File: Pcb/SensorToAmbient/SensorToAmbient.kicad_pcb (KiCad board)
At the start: 2 copper layers, 14 parts, among them J1 Conn_01x04, J2 Conn_01x04, J3 Conn_01x04, J4 Conn_01x06, J5 Conn_01x02, J6 Conn_01x06, J7 Conn_01x04, J8 Conn_01x04, J9 Conn_01x04

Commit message: Making boardedge and spacer holes
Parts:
- added REF**: MountingHole_3mm, Mounting_Holes:MountingHole_3mm, F.Cu at (26.2, 84.6)
- added REF**: MountingHole_3mm, Mounting_Holes:MountingHole_3mm, F.Cu at (67.8, 35.8)
- moved R2 114.0 mm to (42.2, 66.3)
- moved R1 99.0 mm to (42.2, 73.2)
- moved J8 96.8 mm to (61.4, 73.4)
- moved J5 96.3 mm to (45.0, 81.1)
- moved J9 94.7 mm to (61.3, 57.8)
- moved RTC1 92.5 mm to (42.2, 53.1), turned to 90 degrees
- moved J7 90.9 mm to (61.3, 43.6)
- moved 3SB1 77.9 mm to (54.9, 32.4)
- moved J6 74.5 mm to (51.8, 23.3)
- moved DCDC1 73.7 mm to (46.4, 72.3)
- moved J4 67.1 mm to (28.1, 23.3)
- moved J3 63.1 mm to (31.4, 73.5)
- moved J2 55.1 mm to (31.4, 58.3)
- moved J1 53.6 mm to (31.4, 43.2)
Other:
- board outline added: 161.9 x 69.7 mm

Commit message: Complete of footprint layout before first wiring work
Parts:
- removed the J5 at (45.0, 81.1)
- added J7: Conn_01x02, Connectors_JST:JST_XH_S02B-XH-A_02x2.50mm_Angled, F.Cu at (44.9, 78.2)
- J5: renamed from J9; footprint SensorToAmbient:Grove_2mm_4pin_angle2 -> Connectors_JST:JST_XH_S04B-XH-A_04x2.50mm_Angled
- J8: renamed from J4; footprint Connectors_JST:JST_XH_B06B-XH-A_06x2.50mm_Straight -> Connectors_JST:JST_XH_S06B-XH-A_06x2.50mm_Angled
- J9: renamed from J6; footprint Connectors_JST:JST_XH_B06B-XH-A_06x2.50mm_Straight -> Connectors_JST:JST_XH_S06B-XH-A_06x2.50mm_Angled
- moved J8 15.0 mm to (42.5, 27.6), turned to 180 degrees
- moved J9 12.1 mm to (63.2, 27.6), turned to 180 degrees
- moved J5 3.57 mm to (61.2, 61.4), turned to 90 degrees
- moved R1 3.15 mm to (42.1, 70.1)
- moved R2 3.15 mm to (42.1, 63.2)
- moved 3SB1 1.70 mm to (54.8, 34.1)
- moved RTC1 1.56 mm to (42.1, 54.6)
- moved J6 1.00 mm to (62.1, 43.1)
- moved DCDC1 0.75 mm to (46.3, 73.1)
- moved J4 0.72 mm to (62.1, 73.3)
- moved J3 0.09 mm to (31.4, 73.4)
- renumbered J8 to J4, J7 to J6

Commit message: Commit intermediate (before revice part layout for wiring)
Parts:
- removed REF** (x2): MountingHole_3mm, Mounting_Holes:MountingHole_3mm
- moved R2 30.6 mm to (67.2, 80.7), turned to 180 degrees
- moved R1 22.8 mm to (59.5, 84.8)
- turned DCDC1 to 270 degrees
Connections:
- net Net-(DCDC1-Pad1) renamed /PWR_BAT
- J5 pad 1: GND -> /PWR5V
- J5 pad 2: /PWR3.3V -> GND
- J6 pad 1: /PWR5V -> GND
- J6 pad 2: GND -> /PWR3.3V
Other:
- net class Bold added: clearance 0.2, trace_width 0.5, via_dia 0.8, via_drill 0.4
- rule pad_to_mask_clearance: 0.2 -> 0.1
- rule via_min_drill: 0.3 -> 0.4
- rule via_min_size: 0.4 -> 0.8

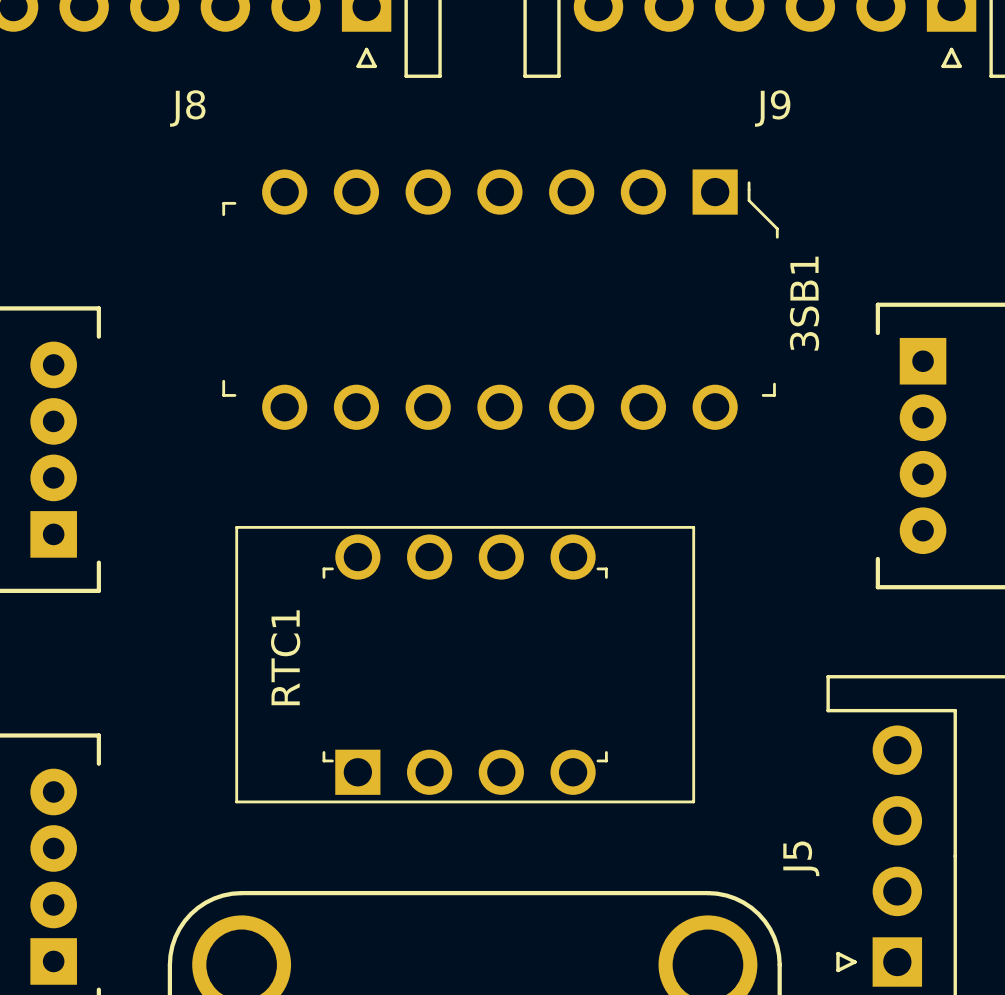
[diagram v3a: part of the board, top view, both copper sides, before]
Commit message: Commit intermediate (Revice schematic for pcb wiring)
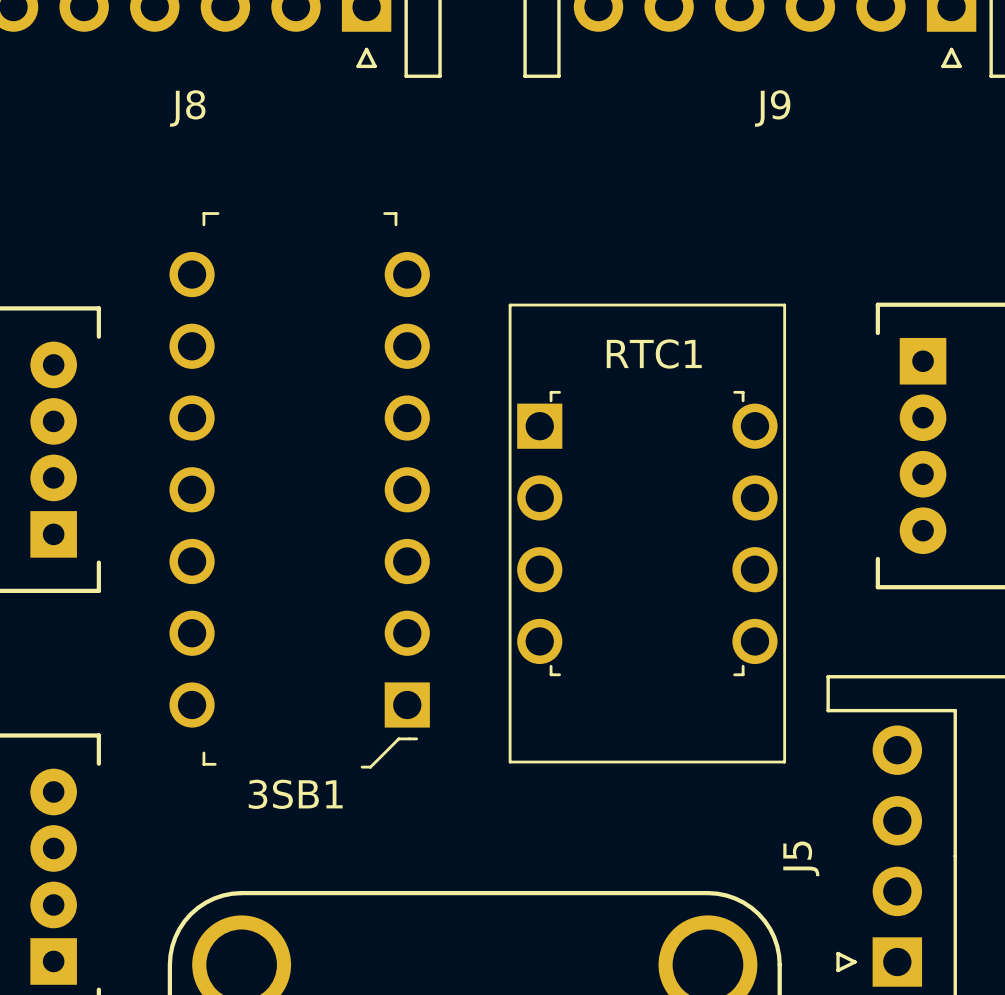
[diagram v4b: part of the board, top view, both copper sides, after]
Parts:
- moved 3SB1 21.2 mm to (43.9, 52.3), turned to 180 degrees
- moved RTC1 13.8 mm to (48.6, 42.4), turned to 0 degrees
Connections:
- 3SB1 pad 14: /PWR3.3V -> Net-(3SB1-Pad14)
- 3SB1 pad 4: Net-(3SB1-Pad1) -> Net-(3SB1-Pad4)
- 3SB1 pad 8: Net-(3SB1-Pad8) -> Net-(3SB1-Pad6)
- J1 pad 1: GND -> Net-(J1-Pad1)
- J1 pad 2: /PWR3.3V -> Net-(J1-Pad2)
- J1 pad 3: Net-(3SB1-Pad3) -> Net-(3SB1-Pad10)
- J1 pad 4: Net-(3SB1-Pad6) -> Net-(J1-Pad4)
- J2 pad 1: GND -> Net-(J2-Pad1)
- J2 pad 2: /PWR3.3V -> Net-(J2-Pad2)
- J3 pad 4: Net-(3SB1-Pad1) -> Net-(3SB1-Pad6)
- J4 pad 1: GND -> Net-(J4-Pad1)
- J4 pad 2: /PWR3.3V -> Net-(J4-Pad2)
- J4 pad 4: Net-(J4-Pad4) -> Net-(3SB1-Pad4)
- J5 pad 1: /PWR5V -> Net-(J5-Pad1)
- J5 pad 2: GND -> Net-(J5-Pad2)
- J5 pad 3: Net-(J5-Pad3) -> /PWR5V
- J5 pad 4: Net-(J5-Pad4) -> GND
- J6 pad 1: GND -> Net-(J6-Pad1)
- J6 pad 2: /PWR3.3V -> Net-(J6-Pad2)
- J6 pad 3: Net-(J5-Pad3) -> Net-(J5-Pad1)
- J6 pad 4: Net-(J5-Pad4) -> Net-(J5-Pad2)
- J8 pad 3: Net-(J3-Pad3) -> Net-(J2-Pad4)
- J8 pad 4: Net-(J2-Pad4) -> Net-(J3-Pad3)
- J8 pad 5: Net-(3SB1-Pad2) -> Net-(3SB1-Pad10)
- J9 pad 3: Net-(J3-Pad3) -> Net-(J2-Pad4)
- J9 pad 4: Net-(J2-Pad4) -> Net-(J3-Pad3)
- RTC1 pad 1: Net-(J4-Pad4) -> Net-(J1-Pad4)
- RTC1 pad 2: Net-(J3-Pad3) -> Net-(J2-Pad4)
- RTC1 pad 5: Net-(J5-Pad3) -> Net-(J5-Pad1)
- RTC1 pad 6: Net-(J5-Pad4) -> Net-(J5-Pad2)
- RTC1 pad 8: /PWR_BAT -> /PWR5V

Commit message: Commit intermediate (Remaining wire is only one GND)
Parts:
- moved R2 23.3 mm to (50.6, 64.4)
- moved R1 17.5 mm to (50.5, 69.8), turned to 180 degrees
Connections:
- 3SB1 pad 14: Net-(3SB1-Pad14) -> GND
- 3SB1 pad 7: GND -> Net-(3SB1-Pad7)
- 3SB1 pad 9: (no net) -> Net-(3SB1-Pad9)
- DCDC1 pad 2: GND -> Net-(3SB1-Pad7)
- DCDC1 pad 5: GND -> Net-(3SB1-Pad7)
- J3 pad 2: /PWR3.3V -> GND
- J5 pad 1: Net-(J5-Pad1) -> GND
- J5 pad 2: Net-(J5-Pad2) -> /PWR5V
- J5 pad 3: /PWR5V -> Net-(J5-Pad3)
- J5 pad 4: GND -> Net-(J5-Pad4)
- J6 pad 3: Net-(J5-Pad1) -> Net-(J5-Pad3)
- J6 pad 4: Net-(J5-Pad2) -> Net-(J5-Pad4)
- J7 pad 1: GND -> /PWR_BAT
- J7 pad 2: /PWR_BAT -> GND
- J8 pad 1: /PWR3.3V -> GND
- J8 pad 5: Net-(3SB1-Pad10) -> Net-(3SB1-Pad9)
- J9 pad 1: /PWR3.3V -> GND
- RTC1 pad 5: Net-(J5-Pad1) -> Net-(J5-Pad3)
- RTC1 pad 6: Net-(J5-Pad2) -> Net-(J5-Pad4)
- RTC1 pad 8: /PWR5V -> /PWR_BAT
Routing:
- net GND: track 0.00 -> 398.9 mm
- net /PWR_BAT: track 0.00 -> 101.0 mm
- net Net-(J2-Pad4): track 0.00 -> 96.9 mm
- net Net-(J3-Pad3): track 0.00 -> 91.5 mm
- net Net-(DCDC1-Pad3): track 0.00 -> 73.7 mm
- net Net-(J2-Pad3): track 0.00 -> 58.6 mm
- net Net-(3SB1-Pad6): track 0.00 -> 52.3 mm
- net Net-(3SB1-Pad4): track 0.00 -> 33.2 mm
- net /PWR5V: track 0.00 -> 30.3 mm
- net Net-(J4-Pad3): track 0.00 -> 27.9 mm
- net Net-(J5-Pad4): track 0.00 -> 26.4 mm
- net Net-(J5-Pad3): track 0.00 -> 22.7 mm
- net Net-(3SB1-Pad5): track 0.00 -> 18.4 mm
- net Net-(3SB1-Pad9): track 0.00 -> 13.6 mm
- net Net-(3SB1-Pad10): track 0.00 -> 5.78 mm

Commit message: First comple of wiring
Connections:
- 3SB1 pad 7: Net-(3SB1-Pad7) -> GND
- 3SB1 pad 8: Net-(3SB1-Pad6) -> Net-(3SB1-Pad11)
- DCDC1 pad 2: Net-(3SB1-Pad7) -> Net-(DCDC1-Pad2)
- DCDC1 pad 5: Net-(3SB1-Pad7) -> Net-(DCDC1-Pad2)
- J1 pad 3: Net-(3SB1-Pad10) -> Net-(3SB1-Pad13)
- J3 pad 4: Net-(3SB1-Pad6) -> Net-(3SB1-Pad11)
- J4 pad 4: Net-(3SB1-Pad4) -> Net-(3SB1-Pad10)
- J8 pad 5: Net-(3SB1-Pad9) -> Net-(3SB1-Pad12)
- J9 pad 5: Net-(3SB1-Pad5) -> Net-(3SB1-Pad9)
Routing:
- net Net-(3SB1-Pad6): track 52.3 -> 0.00 mm
- net Net-(3SB1-Pad11): track 0.00 -> 44.5 mm
- net Net-(3SB1-Pad10): track 5.78 -> 40.1 mm
- net Net-(3SB1-Pad4): track 33.2 -> 1.13 mm
- net Net-(3SB1-Pad12): track 0.00 -> 21.2 mm
- net Net-(3SB1-Pad5): track 18.4 -> 0.00 mm
- net GND: track 398.9 -> 413.9 mm
- net Net-(3SB1-Pad9): track 13.6 -> 21.9 mm
- net Net-(3SB1-Pad13): track 0.00 -> 7.53 mm
- net Net-(J3-Pad3): track 91.5 -> 96.9 mm

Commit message: Fix DRC errors
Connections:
- 3SB1 pad 14: GND -> /PWR3.3V
- DCDC1 pad 2: Net-(DCDC1-Pad2) -> GND
- DCDC1 pad 5: Net-(DCDC1-Pad2) -> GND
- J3 pad 2: GND -> /PWR3.3V
- J8 pad 1: GND -> /PWR3.3V
- J9 pad 1: GND -> /PWR3.3V
- RTC1 pad 1: Net-(J1-Pad4) -> Net-(RTC1-Pad1)
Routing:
- net /PWR3.3V: track 0.00 -> 124.5 mm
- net GND: track 413.9 -> 290.6 mm
